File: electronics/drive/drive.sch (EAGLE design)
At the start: 11 parts, among them IC1 MEGA8-AI, IC2 MAX1483ESA, J1 AVR_SPI_PRG_6NS

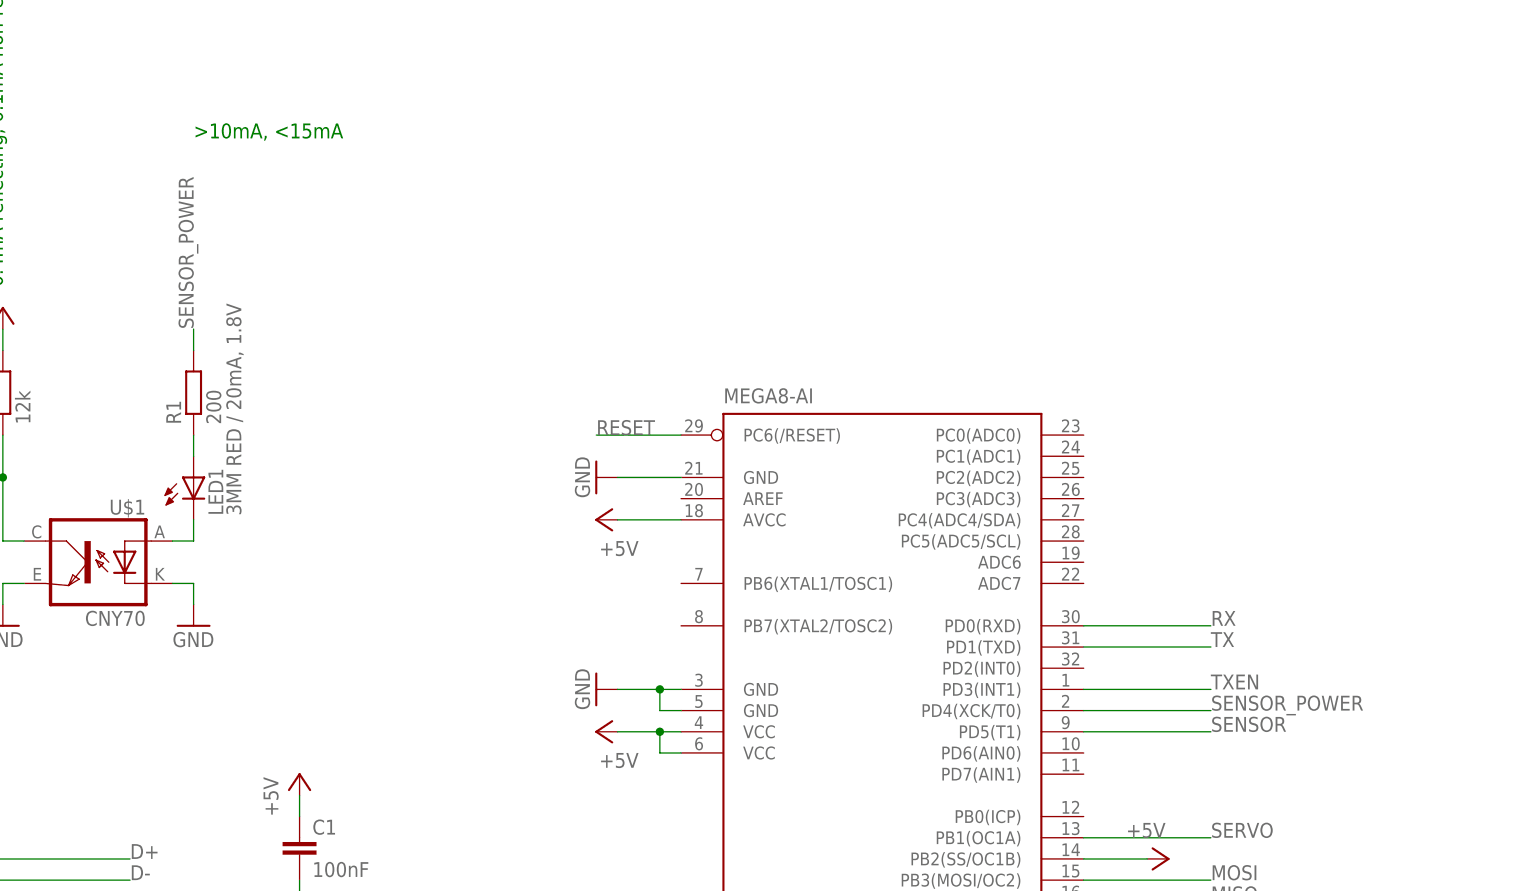
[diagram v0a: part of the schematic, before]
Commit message: Fixing a bug in drive board design.
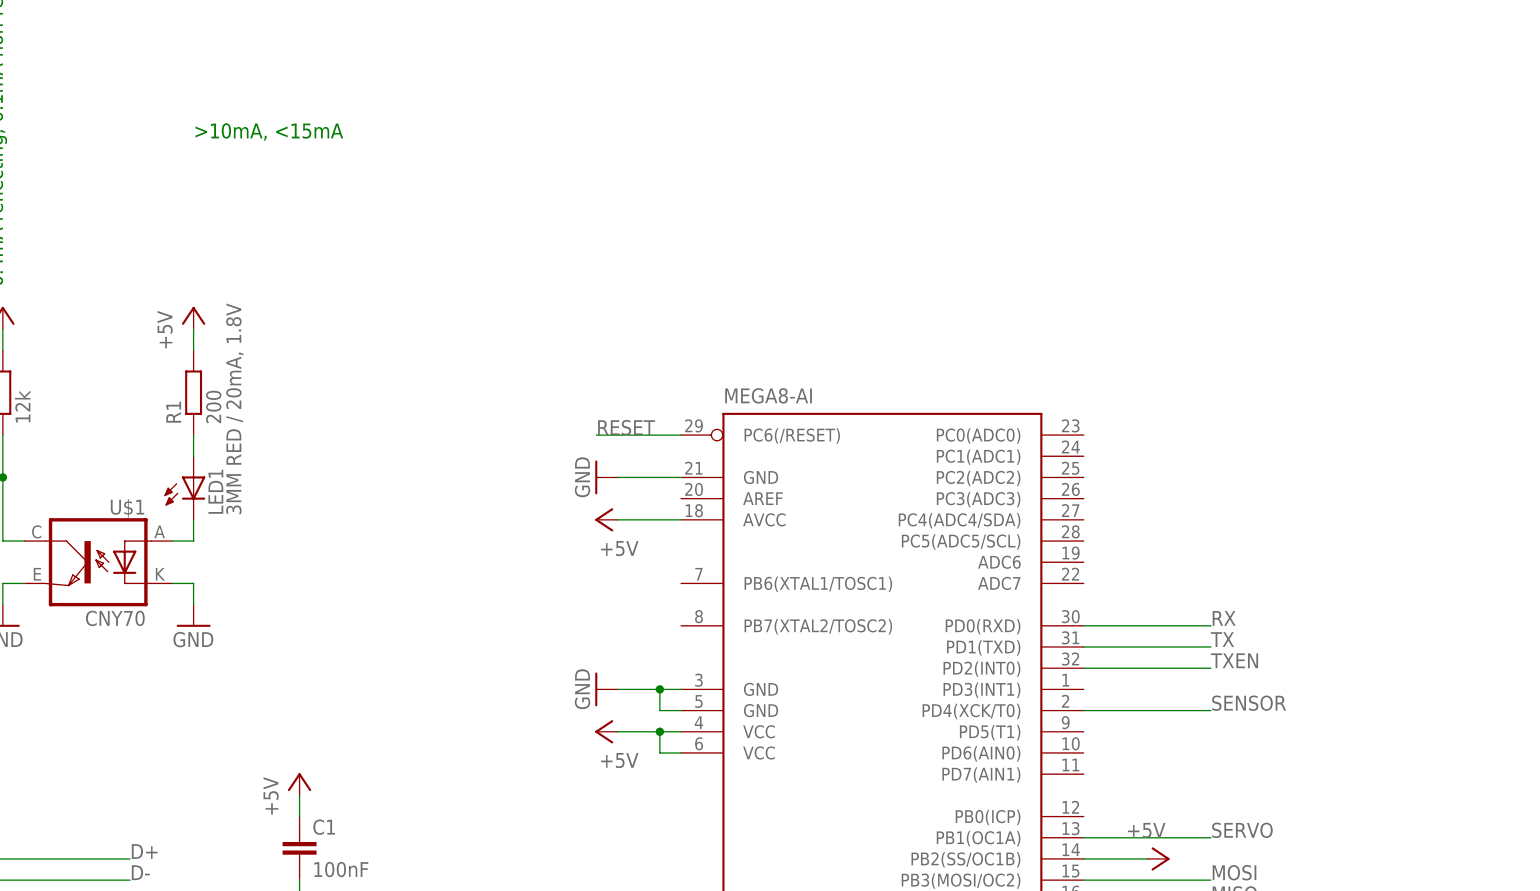
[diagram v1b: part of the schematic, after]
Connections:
- removed net SENSOR_POWER: IC1.PD4(XCK/T0), R1.2
- net +5V: now also R1.2
- net SENSOR: now also IC1.PD4(XCK/T0); no longer IC1.PD5(T1)
- net TXEN: now also IC1.PD2(INT0); no longer IC1.PD3(INT1)
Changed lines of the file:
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@@
 <part name="P+6" library="supply1" deviceset="+5V" device=""/>
 <part name="R3" library="rcl" deviceset="R-EU_" device="R0805" value="1k"/>
+<part name="P+9" library="supply1" deviceset="+5V" device=""/>
 </parts>
 <sheets>
@@
 <instance part="P+6" gate="1" x="-17.78" y="96.52"/>
 <instance part="R3" gate="G$1" x="-12.7" y="7.62" rot="R180"/>
+<instance part="P+9" gate="1" x="5.08" y="96.52"/>
 </instances>
 <busses>
 </busses>
 <nets>
-<net name="SENSOR_POWER" class="0">
-<segment>
-<wire x1="5.08" y1="91.44" x2="5.08" y2="93.98" width="0.1524" layer="91"/>
-<label x="5.08" y="93.98" size="1.778" layer="95" rot="R90"/>
-<pinref part="R1" gate="G$1" pin="2"/>
-</segment>
-<segment>
-<wire x1="111.76" y1="48.26" x2="127" y2="48.26" width="0.1524" layer="91"/>
-<label x="127" y="48.26" size="1.778" layer="95"/>
-<pinref part="IC1" gate="G$1" pin="PD4(XCK/T0)"/>
-</segment>
-</net>
 <net name="SENSOR" class="0">
 <segment>
@@
 </segment>
 <segment>
-<wire x1="111.76" y1="45.72" x2="127" y2="45.72" width="0.1524" layer="91"/>
-<label x="127" y="45.72" size="1.778" layer="95"/>
-<pinref part="IC1" gate="G$1" pin="PD5(T1)"/>
+<wire x1="111.76" y1="48.26" x2="127" y2="48.26" width="0.1524" layer="91"/>
+<label x="127" y="48.26" size="1.778" layer="95"/>
+<pinref part="IC1" gate="G$1" pin="PD4(XCK/T0)"/>
 </segment>
 </net>
@@
 <pinref part="P+6" gate="1" pin="+5V"/>
 <pinref part="R2" gate="G$1" pin="2"/>
+</segment>
+<segment>
+<wire x1="5.08" y1="91.44" x2="5.08" y2="93.98" width="0.1524" layer="91"/>
+<pinref part="R1" gate="G$1" pin="2"/>
+<pinref part="P+9" gate="1" pin="+5V"/>
 </segment>
 </net>
@@
 </segment>
 <segment>
-<wire x1="111.76" y1="50.8" x2="127" y2="50.8" width="0.1524" layer="91"/>
-<label x="127" y="50.8" size="1.778" layer="95"/>
-<pinref part="IC1" gate="G$1" pin="PD3(INT1)"/>
+<pinref part="IC1" gate="G$1" pin="PD2(INT0)"/>
+<wire x1="111.76" y1="53.34" x2="127" y2="53.34" width="0.1524" layer="91"/>
+<label x="127" y="53.34" size="1.778" layer="95"/>
 </segment>
 </net>
@@
 </sheet>
 </sheets>
+<errors>
+</errors>
 </schematic>
 </drawing>

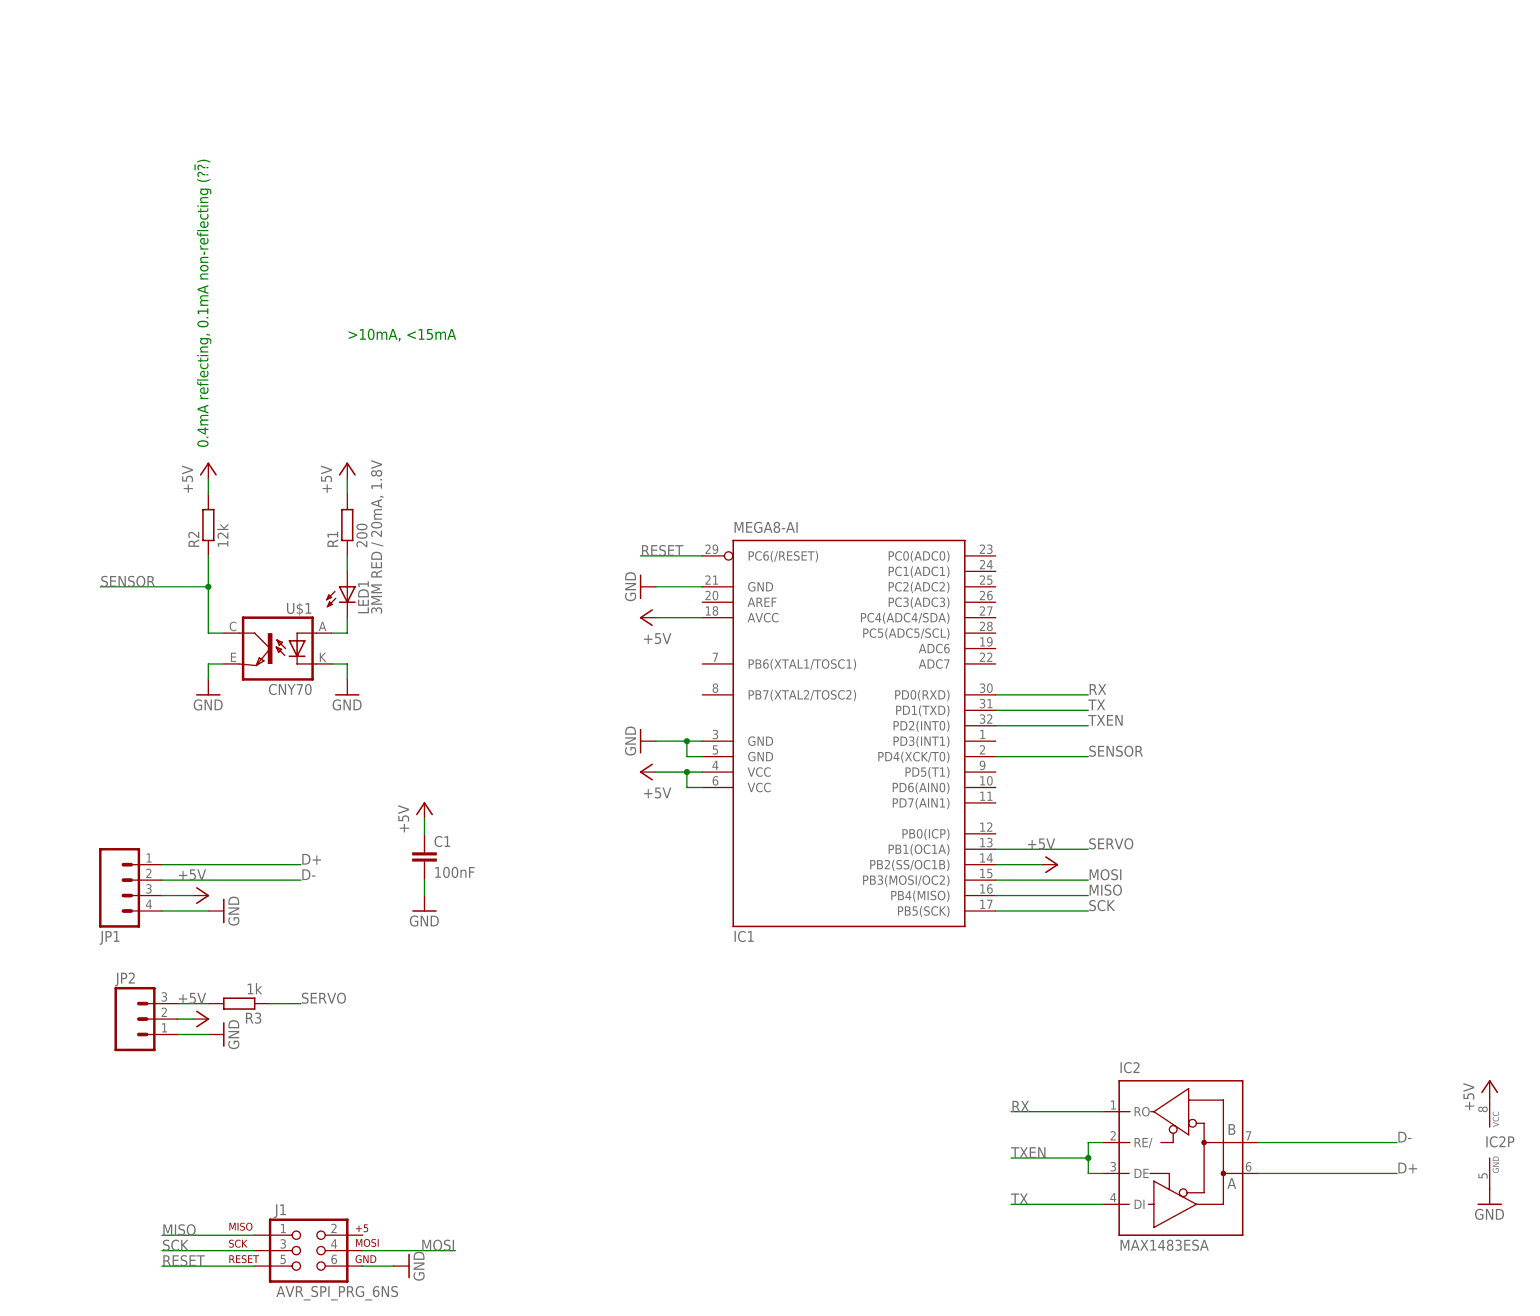
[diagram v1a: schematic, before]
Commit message: First attempt on making the drive board compatible with my soldering skills.
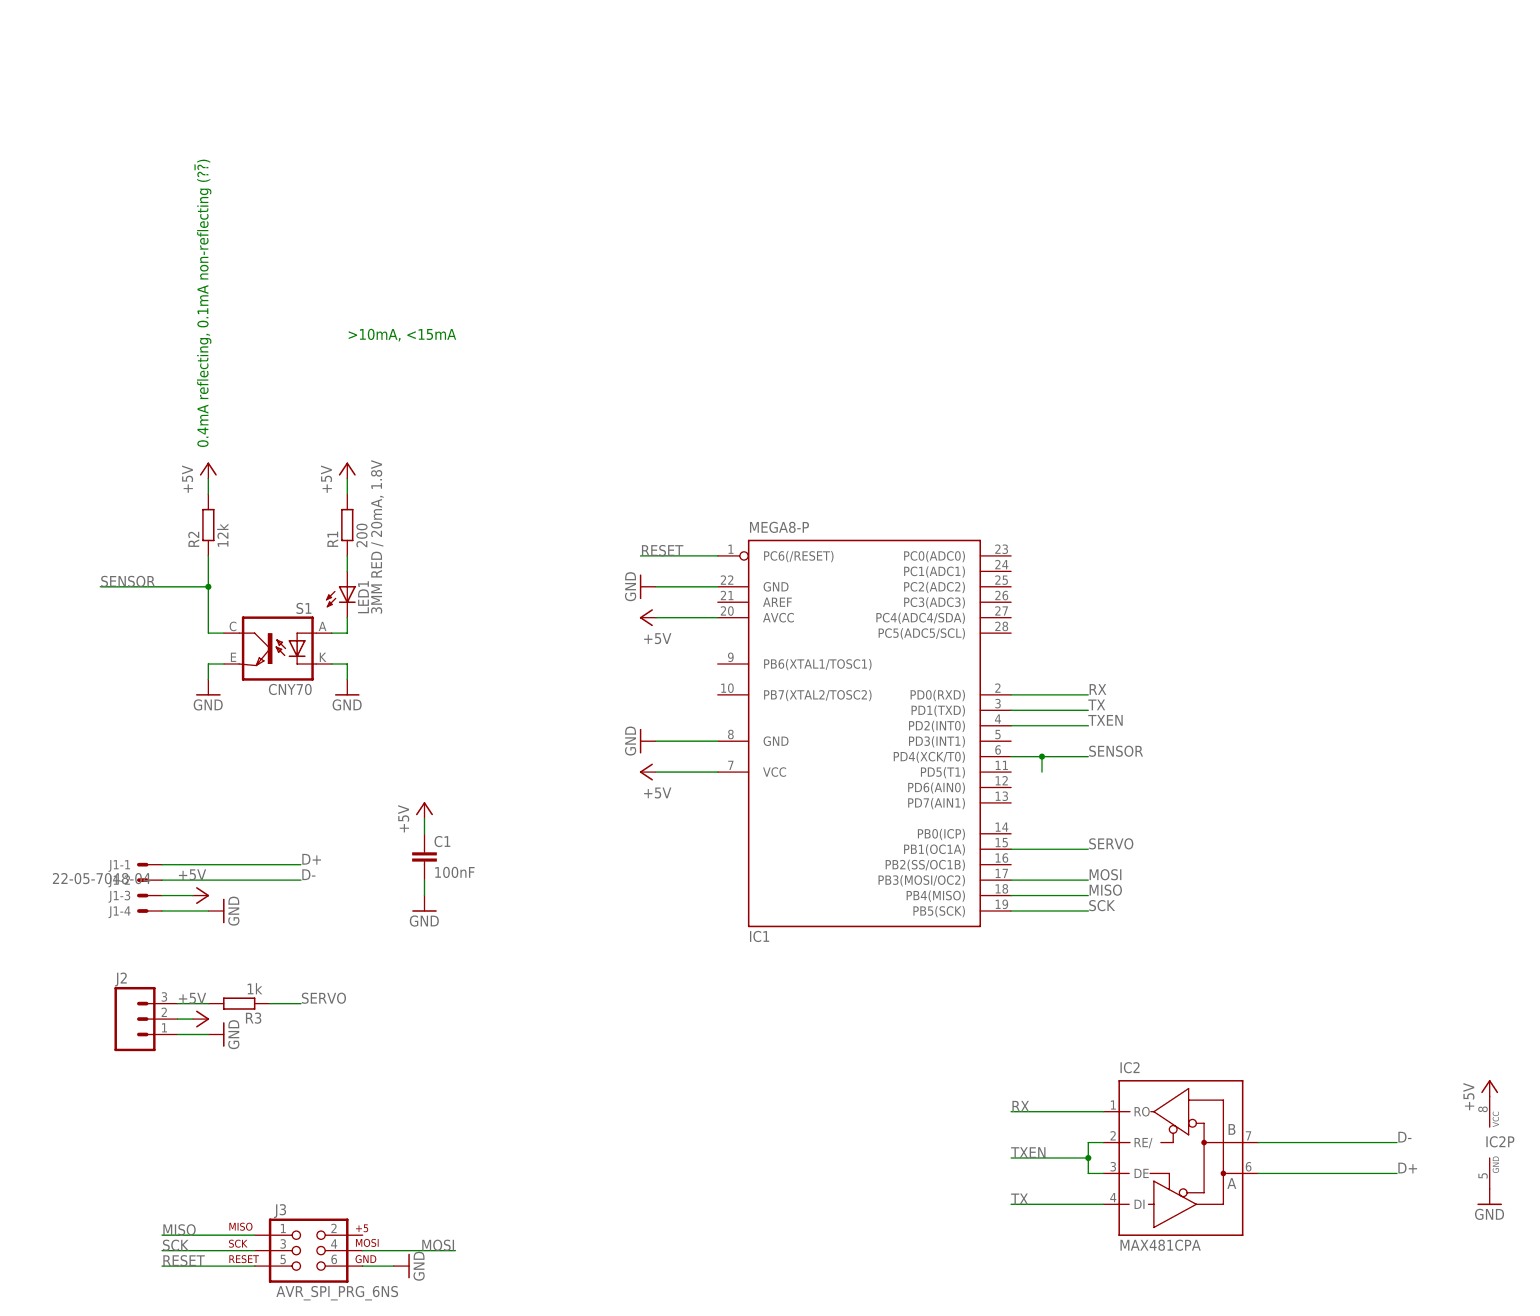
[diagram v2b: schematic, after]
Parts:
- removed JP1: (no value), SparkFun:M04POLAR
- added J3: AVR_SPI_PRG_6NS, SparkFun:AVR_SPI_PRG_6NS
- IC1: value MEGA8-AI -> MEGA8-P; device atmel:MEGA8-AI -> atmel:MEGA8-P
- IC2: value MAX1483ESA -> MAX481CPA; device maxim:MAX481CSA -> maxim:MAX481CPA
- J1: value AVR_SPI_PRG_6NS -> 22-05-7048-04; device SparkFun:AVR_SPI_PRG_6NS -> con-molex:22-05-7048-04
- LED1: device led:LED3MM -> led:LEDCHIP-LED0805
- renumbered JP2 to J2, U$1 to S1
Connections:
- net +5V: now also J1-3.S; no longer IC1.PB2(SS/OC1B), IC1.VCC@2, JP1.3
- net D+: now also J1-1.S; no longer JP1.1
- net D-: now also J1-2.S; no longer JP1.2
- net GND: now also J1-4.S, J3.6; no longer IC1.GND@2, J1.6, JP1.4
- net MISO: now also J3.1; no longer J1.1
- net MOSI: now also J3.4; no longer J1.4
- net RESET: now also J3.5; no longer J1.5
- net SCK: now also J3.3; no longer J1.3
